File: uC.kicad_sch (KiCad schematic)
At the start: 52 parts, among them J401 Conn_02x05_Counter_Clockwise, J402 Conn_02x05_Counter_Clockwise, J403 Conn_02x08_Counter_Clockwise, SW401 SW_Push, SW402 SW_Push, U401 STM32F103RGT6, U402 BLUENRG-M2SA, Y401 16MHz, Y402 32.768KHz

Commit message: v2.0 schematics updated
1. Need to be tested for errors
2. PCB layout is not started yet
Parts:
- removed C401, C402, C403, C404, C407, C414, C415, C419: 100n, Capacitor_SMD:C_0402_1005Metric, symbol Device:C
- removed C410, C411: 1u, Capacitor_SMD:C_0402_1005Metric, symbol Device:C
- removed C412: 10n, Capacitor_SMD:C_0402_1005Metric, symbol Device:C
- removed C416: 10u, Capacitor_SMD:C_0603_1608Metric, symbol Device:C
- removed C417, C420: 6p8, Capacitor_SMD:C_0402_1005Metric, symbol Device:C
- removed C418, C421: 5p6, Capacitor_SMD:C_0402_1005Metric, symbol Device:C
- removed D401, D402: ESDALC6V1-1M2, EMS:ESDALC6V11M2, symbol EMS:ESDALC6V1-1M2
- removed D403, D404, D405, D406, D407: PESD3V3L1BA,115, EMS:PESD3V3L1BA_115-SOD-323-2, symbol EMS:PESD3V3L1BA,115
- removed D408: LED_RAGB, LED_SMD:LED_Kingbright_APFA3010_3x1.5mm_Horizontal, symbol Device:LED_RAGB
- removed J401: Conn_02x05_Counter_Clockwise, EMS:62701021621, symbol Connector_Generic:Conn_02x05_Odd_Even
- removed L401: 10n, Inductor_SMD:L_0603_1608Metric, symbol Device:L
- removed R401, R402, R403, R404: 49R9, Resistor_SMD:R_0402_1005Metric, symbol Device:R
- removed R405: 10k, Resistor_SMD:R_0603_1608Metric, symbol Device:R
- removed R408, R409: 22R, Resistor_SMD:R_0603_1608Metric, symbol Device:R
- removed R411, R412, R413: 1k, Resistor_SMD:R_0603_1608Metric, symbol Device:R
- removed SW401, SW402: SW_Push, Button_Switch_SMD:SW_SPST_CK_RS282G05A3, symbol Switch:SW_Push
- removed U401: STM32F103RGT6, EMS:STM32F103RGT6-LQFP-64, symbol EMS:STM32F103RGT6
- removed Y401: 16MHz, Crystal:Crystal_SMD_3225-4Pin_3.2x2.5mm, symbol Device:Crystal_GND24
- removed Y402: 32.768KHz, Crystal:Crystal_SMD_3215-2Pin_3.2x1.5mm, symbol Device:Crystal
- added C506, C507: 100n, Capacitor_SMD:C_0402_1005Metric, symbol Device:C
- added D501: ESDALC6V1-1M2, EMS:ESDALC6V11M2, symbol EMS:ESDALC6V1-1M2
- added J503: CLP-110-02-G-D, EMS:CLP-110-02-XXX-D, symbol EMS:CLP-110-02-G-D
- added SW501: SW_Push, Button_Switch_SMD:SW_SPST_CK_RS282G05A3, symbol Switch:SW_Push
- renumbered C408 to C501, C409 to C502, C413 to C503, C405 to C504, C406 to C505, J402 to J501, J403 to J502, R406 to R501, R407 to R502, R410 to R503, U402 to U501
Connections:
- net ADC1_IN10 is gone; now on net GND: J502.6 (Pin_6)
- net ADC1_IN9 is gone; now on net +DCDC_2: J502.4 (Pin_4)
- net DAC_OUT1 is gone; now on net +DCDC_1: J502.2 (Pin_2)
- net GPIO1_Output is gone; now on net ADS_CS: J502.18 (Pin_18)
- net +DCDC_1: no longer J502.10 (Pin_10)
- net +DCDC_2: now also C506.1, J503.10; no longer J502.12 (Pin_12)
- net ADS_CS: no longer J502.15 (Pin_15)
- net ADS_DIN_uC_DOUT: now also J502.16 (Pin_16); no longer J502.13 (Pin_13)
- net ADS_DOUT_uC_DIN: now also J502.14 (Pin_14); no longer J502.11 (Pin_11)
- net ADS_SPI1_SCK: now also J502.12 (Pin_12); no longer J502.9 (Pin_9)
- net BLE_RST: now also C507.1, D501.1 (K), SW501.1
- net GND: now also C506.2, C507.2, D501.2 (A), J503.8, SW501.2; no longer J502.8 (Pin_8)
- net I2C1_SCL: now also J503.15; no longer J502.16 (Pin_16)
- net I2C1_SDA: now also J503.13; no longer J502.14 (Pin_14)
- net BLE_SPI_CS renamed SPI5_CS
- net GPIO1_Input: no longer names the net of J502.17 (Pin_17)
- net GPIO2_Input: no longer names the net of J502.19 (Pin_19)
- net SPI2_MISO renamed SPI5_MISO
- net SPI2_MOSI renamed SPI5_MOSI
- net SPI2_R_MISO: no longer names the net of R502.2, U501.16 (DIO2)
- net SPI2_SCK renamed SPI5_SCK
- new net ADC1_INP9: J503.11
- new net ADC3_INP1: J503.9
- new net FDCAN2_RX: J503.16
- new net FDCAN2_TX: J503.18
- new net GPIO_IN_1: J503.19
- new net GPIO_IN_2: J503.17
- new net GPIO_OUT_1: J503.20
- new net SPI1_MISO: J503.1
- new net SPI1_MOSI: J503.3
- new net SPI1_NSS: J503.7
- new net SPI1_SCK: J503.5
- new net TIM4_CH1: J503.14
- new net TIM4_CH2: J503.12
- new net UART4_DE: J503.4
- new net UART4_RX: J503.6
- new net UART4_TX: J503.2
- no-connect marks 16 -> 19
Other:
- note added: "Board-to-board"
- note added: "Connectors"
- note added: "Simple Connector"
- note added: "[2] BLE"
- note removed: "BOOT0"
- note removed: "Bulk Decoupling Capacitor"
- note removed: "Crystal Oscillator"
- note removed: "MCU - STM32F103RGT6"
- note removed: "RGB LED"
- note removed: "SWD Header"
- note removed: "Switch - RESET & BOOT0"
- note removed: "[2] MCU"
- moved on the sheet: C501, C502, C503, C504, C505, J501, J502, R501, R502, R503, U501

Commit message: minor formatting updates
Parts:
- removed C507: 100n, Capacitor_SMD:C_0402_1005Metric, symbol Device:C
- removed D501: ESDALC6V1-1M2, EMS:ESDALC6V11M2, symbol EMS:ESDALC6V1-1M2
- removed SW501: SW_Push, Button_Switch_SMD:SW_SPST_CK_RS282G05A3, symbol Switch:SW_Push
- renumbered C506 to C505, C505 to C506, J503 to J501, J501 to J502, J502 to J503, R503 to R501, R501 to R503
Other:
- note removed: "RESET"
- moved on the sheet: C504, C505, C506, J501, J502, J503

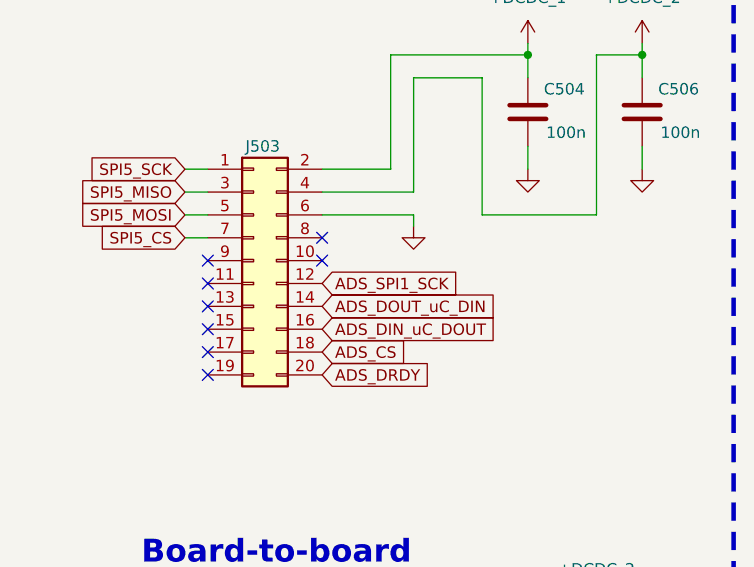
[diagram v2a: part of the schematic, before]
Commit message: schematics errors fixed and ready for PCB
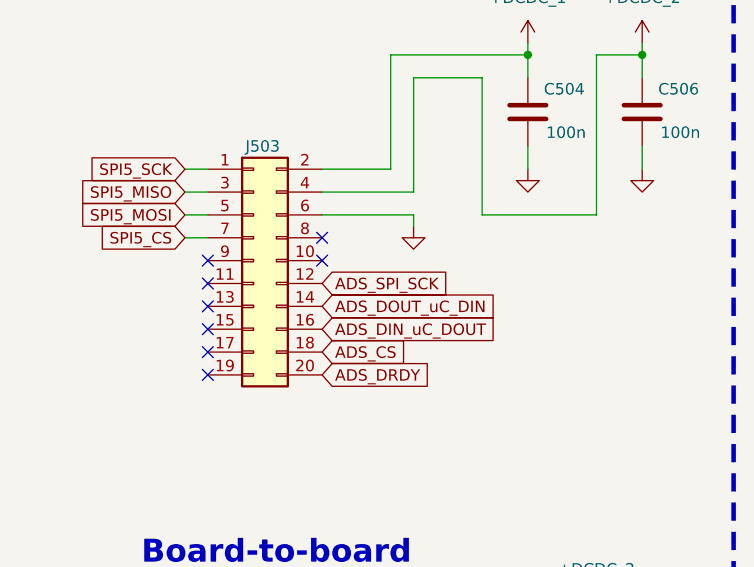
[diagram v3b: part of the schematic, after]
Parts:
- C501: Manufacturer_Part_Number KGM05AR51A225KH -> 04023C104KAT2A
- J501: Distributor_Link (none) -> https://www.mouser.com/ProductDetail/Samtec/CLP-110-02-G-D?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
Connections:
- net ADS_SPI1_SCK renamed ADS_SPI_SCK
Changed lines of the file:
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@@
 		)
 	)
+	(global_label "ADS_SPI_SCK"
+		(shape input)
+		(at 222.25 144.78 0)
+		(fields_autoplaced yes)
+		(effects
+			(font
+				(size 1.27 1.27)
+			)
+			(justify left)
+		)
+		(property "Intersheetrefs" "${INTERSHEET_REFS}"
+			(at 237.5723 144.78 0)
+			(effects
+				(font
+					(size 1.27 1.27)
+				)
+				(justify left)
+				(hide yes)
+			)
+		)
+	)
 	(global_label "I2C1_SCL"
 		(shape input)
@@
 		)
 	)
-	(global_label "ADS_SPI1_SCK"
-		(shape input)
-		(at 222.25 144.78 0)
-		(fields_autoplaced yes)
-		(effects
-			(font
-				(size 1.27 1.27)
-			)
-			(justify left)
-		)
-		(property "Intersheetrefs" "${INTERSHEET_REFS}"
-			(at 238.7818 144.78 0)
-			(effects
-				(font
-					(size 1.27 1.27)
-				)
-				(justify left)
-				(hide yes)
-			)
-		)
-	)
 	(global_label "GPIO_OUT_1"
 		(shape input)
@@
 			)
 		)
-		(property "Datasheet" "https://www.mouser.com/datasheet/2/40/cx5r_KGM-3223198.pdf"
+		(property "Datasheet" "https://www.mouser.com/datasheet/2/40/KGM_X7R-3223212.pdf"
 			(at 45.72 96.52 0)
 			(effects
@@
 			)
 		)
-		(property "Manufacturer_Part_Number" "KGM05AR51A225KH"
+		(property "Manufacturer_Part_Number" "04023C104KAT2A"
 			(at 45.72 96.52 0)
 			(effects
@@
 				(hide yes)
 			)
+		)
+		(property "Distributor_Link" "https://www.mouser.com/ProductDetail/Samtec/CLP-110-02-G-D?qs=0lQeLiL1qyaw0wV0yc599g%3D%3D"
+			(at 205.74 187.96 0)
+			(effects
+				(font
+					(size 1.27 1.27)
+				)
+				(hide yes)
+			)

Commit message: new version created. Now at v2.0.0
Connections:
- net SPI5_MISO_R: now reaches R502.2, U501.16 (DIO2)
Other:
- moved on the sheet: R502
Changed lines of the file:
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@@
+	)
+	(junction
+		(at 132.08 123.19)
+		(diameter 0)
+		(color 0 0 0 0)
 	)
 	(junction
@@
 	(wire
 		(pts
+			(xy 132.08 110.49) (xy 132.08 123.19)
+		)
+		(stroke
+			(width 0)
+			(type default)
+		)
+	)
+	(wire
+		(pts
 			(xy 104.14 161.29) (xy 104.14 153.67)
 		)
@@
 	(wire
 		(pts
-			(xy 139.7 123.19) (xy 146.05 123.19)
+			(xy 144.78 123.19) (xy 146.05 123.19)
 		)
 		(stroke
@@
 		(pts
 			(xy 229.87 119.38) (xy 245.11 119.38)
+		)
+		(stroke
+			(width 0)
+			(type default)
+		)
+	)
+	(wire
+		(pts
+			(xy 135.89 110.49) (xy 132.08 110.49)
+		)
+		(stroke
+			(width 0)
+			(type default)
+		)
+	)
+	(wire
+		(pts
+			(xy 132.08 123.19) (xy 137.16 123.19)
 		)
 		(stroke
@@
 				(bold yes)
 			)
+		)
+	)
+	(label "SPI5_MISO_R"
+		(at 135.89 110.49 0)
+		(fields_autoplaced yes)
+		(effects
+			(font
+				(size 1.27 1.27)
+			)
+			(justify left bottom)
 		)
 	)
@@
 	(symbol
 		(lib_id "Device:R")
-		(at 135.89 123.19 270)
+		(at 140.97 123.19 270)
 		(unit 1)
 		(exclude_from_sim no)
@@
 		(dnp no)
 		(property "Reference" "R502"
-			(at 138.176 121.666 90)
+			(at 143.256 121.666 90)
 			(effects
 				(font
@@
 		)
 		(property "Value" "22R"
-			(at 137.668 123.19 90)
+			(at 142.748 123.19 90)
 			(effects
 				(font
@@
 		)
 		(property "Footprint" "Resistor_SMD:R_0603_1608Metric"
-			(at 135.89 121.412 90)
+			(at 140.97 121.412 90)
 			(effects
 				(font
@@
 		)
 		(property "Datasheet" "https://www.mouser.com/datasheet/2/315/AOA0000C334-1314047.pdf"
-			(at 135.89 123.19 0)
+			(at 140.97 123.19 0)
 			(effects
 				(font
@@
 		)
 		(property "Description" "Resistor"
-			(at 135.89 123.19 0)
+			(at 140.97 123.19 0)
 			(effects
 				(font
@@
 		)
 		(property "Arrow Part Number" ""
-			(at 135.89 123.19 0)
+			(at 140.97 123.19 0)
 			(effects
 				(font
@@
 		)
 		(property "Arrow Price/Stock" ""
-			(at 135.89 123.19 0)
+			(at 140.97 123.19 0)
 			(effects
 				(font
@@
 		)
 		(property "Distributor_Link" "https://www.mouser.com/ProductDetail/Panasonic/ERJ-S03F22R0V?qs=sGAEpiMZZMvdGkrng054t59%2FMXCyyixeZfkxx1NkMqo%3D"
-			(at 135.89 123.19 0)
+			(at 140.97 123.19 0)
 			(effects
 				(font
@@
 		)
 		(property "Manufacturer_Name" "Panasonic"
-			(at 135.89 123.19 0)
+			(at 140.97 123.19 0)
 			(effects
 				(font
@@
 		)
 		(property "Manufacturer_Part_Number" "ERJ-S03F22R0V"
-			(at 135.89 123.19 0)
-			(effects
-				(font
+			(at 140.97 123.19 0)
+			(effects
+				(font

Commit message: minor design improvements
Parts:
- C501: Manufacturer_Part_Number 04023C104KAT2A -> KGM05AR51A225KH
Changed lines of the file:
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@@
 			)
 		)
-		(property "Manufacturer_Part_Number" "04023C104KAT2A"
+		(property "Manufacturer_Part_Number" "KGM05AR51A225KH"
 			(at 45.72 96.52 0)
 			(effects
